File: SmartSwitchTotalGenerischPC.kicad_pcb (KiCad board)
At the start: 2 copper layers, 20.4 x 30.8 mm, 16 parts, among them IC1 AQW282SZ, J1 Conn_02x05_Odd_Even, J2 Conn_02x05_Odd_Even, J3 Conn_02x06_Odd_Even, U1 XIAO-ESP32-C6

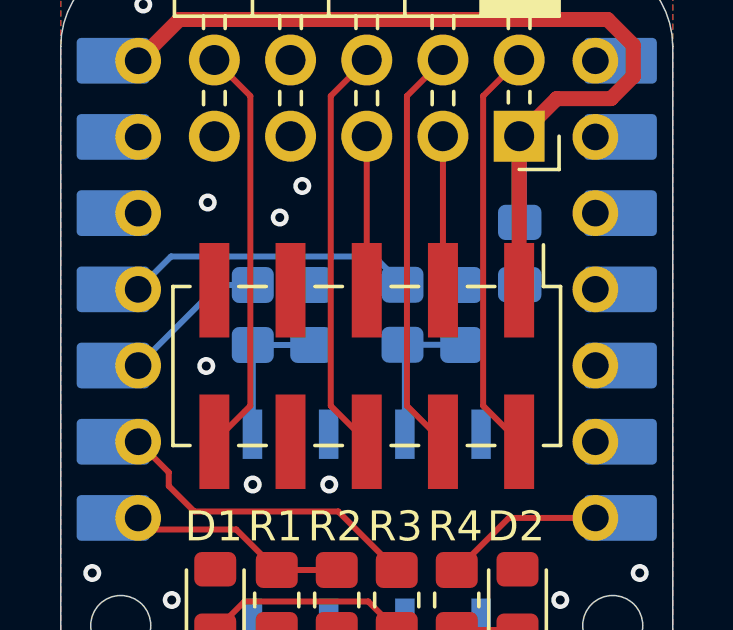
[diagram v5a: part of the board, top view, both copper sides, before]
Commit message: removed: pulldown resistor from switching circuit
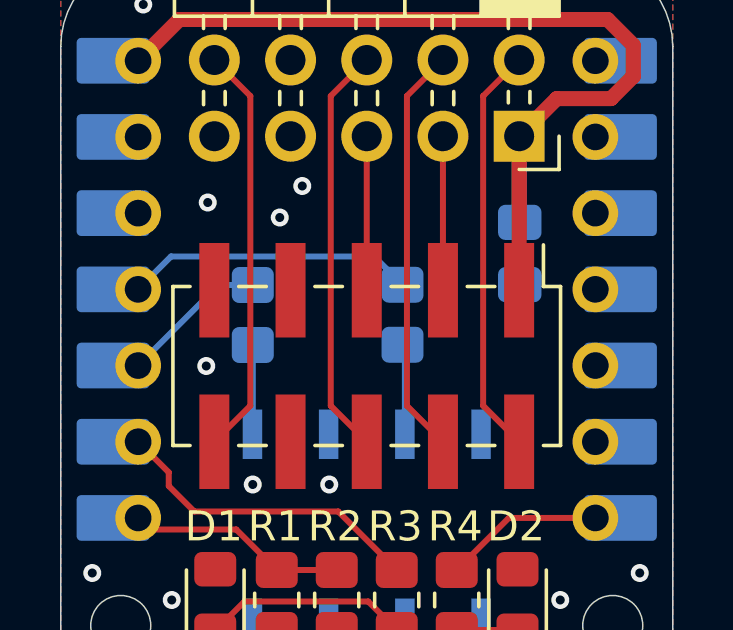
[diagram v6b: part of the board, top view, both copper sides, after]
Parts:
- removed R7, R8: 10k, Resistor_SMD:R_0805_2012Metric_Pad1.20x1.40mm_HandSolder
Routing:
- net Net-(IC1-A2): track 4.98 -> 3.01 mm
- net Net-(IC1-A1): track 4.93 -> 2.98 mm
